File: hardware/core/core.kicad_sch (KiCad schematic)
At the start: 66 parts, among them IC1 LD1117-3.3V-SOT223, J1 9V_IN, J2 MIDI IN, J3 MIDI OUT 1, J4 MIDI OUT 2, J5 MIDI OUT 3, J6 MIDI OUT 4, J7 LCD, J8 USB_C_Receptacle_USB2.0_16P, SW1 FS, SW10 BOOT, SW2 FS, SW3 FS, SW4 FS, SW5 FS, SW6 FS, SW7 FS, SW8 FS, SW9 RESET, U1 LM2596S-5, U2 6N137, U3 ESP32-S3-WROOM-1, U5 USBLC6-2SC6

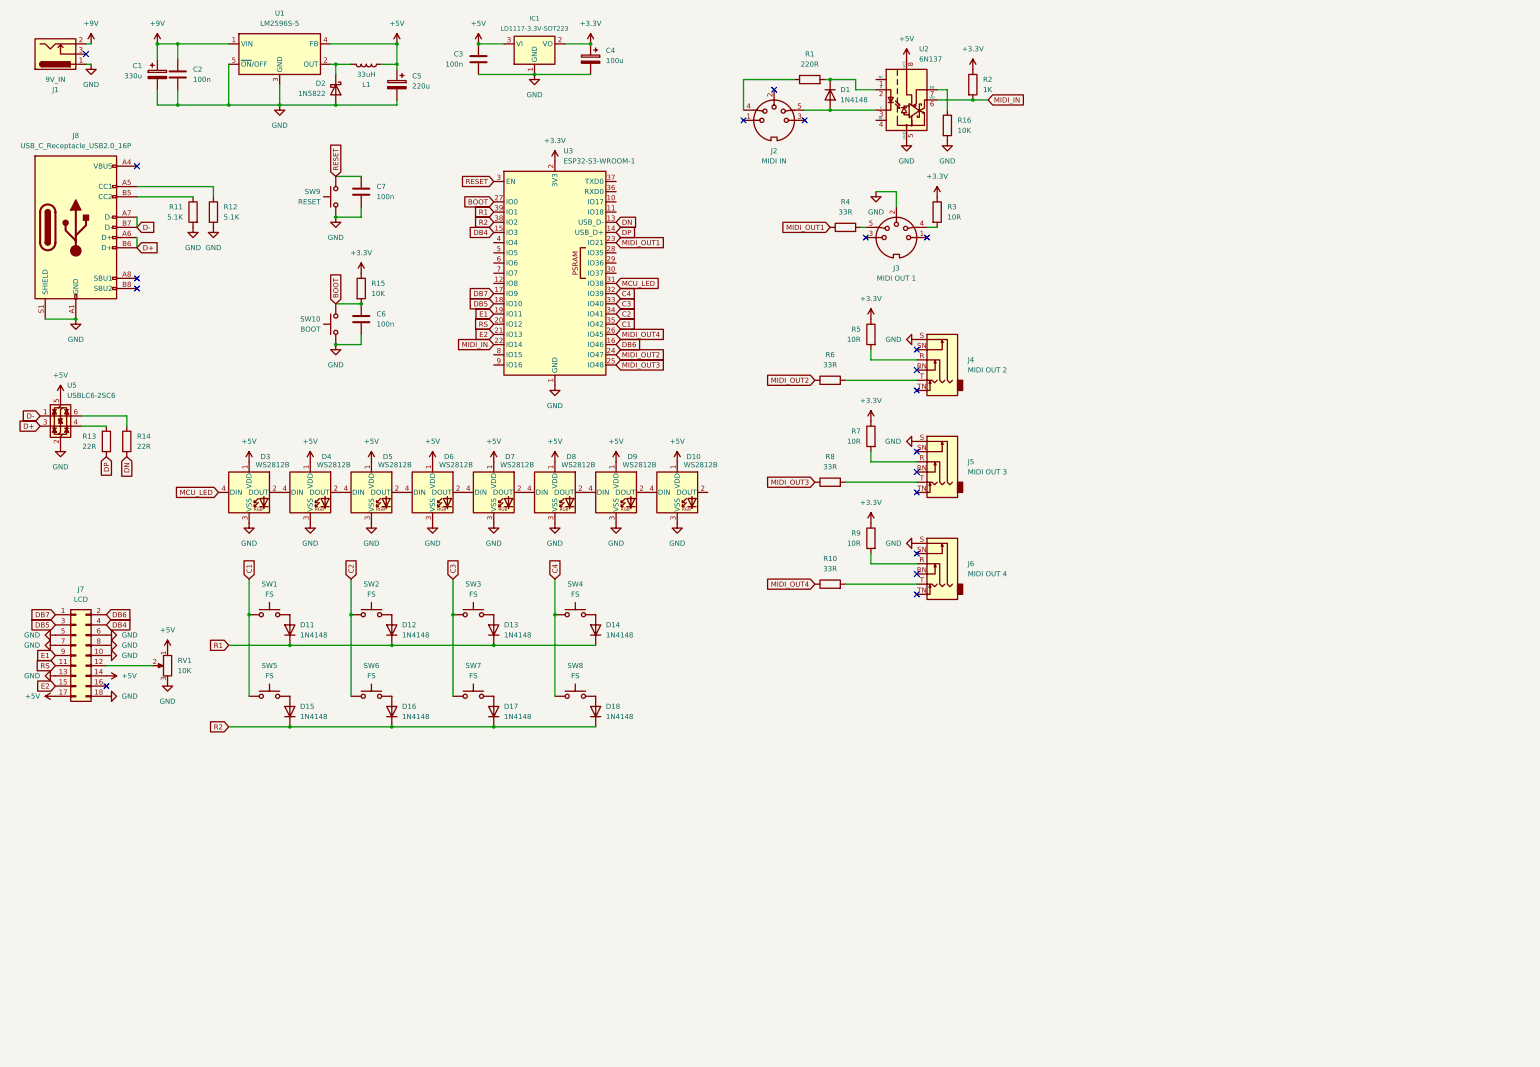
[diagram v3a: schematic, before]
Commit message: Add WS2812B LED support, update LCD pinout docs, and revise PCB nets
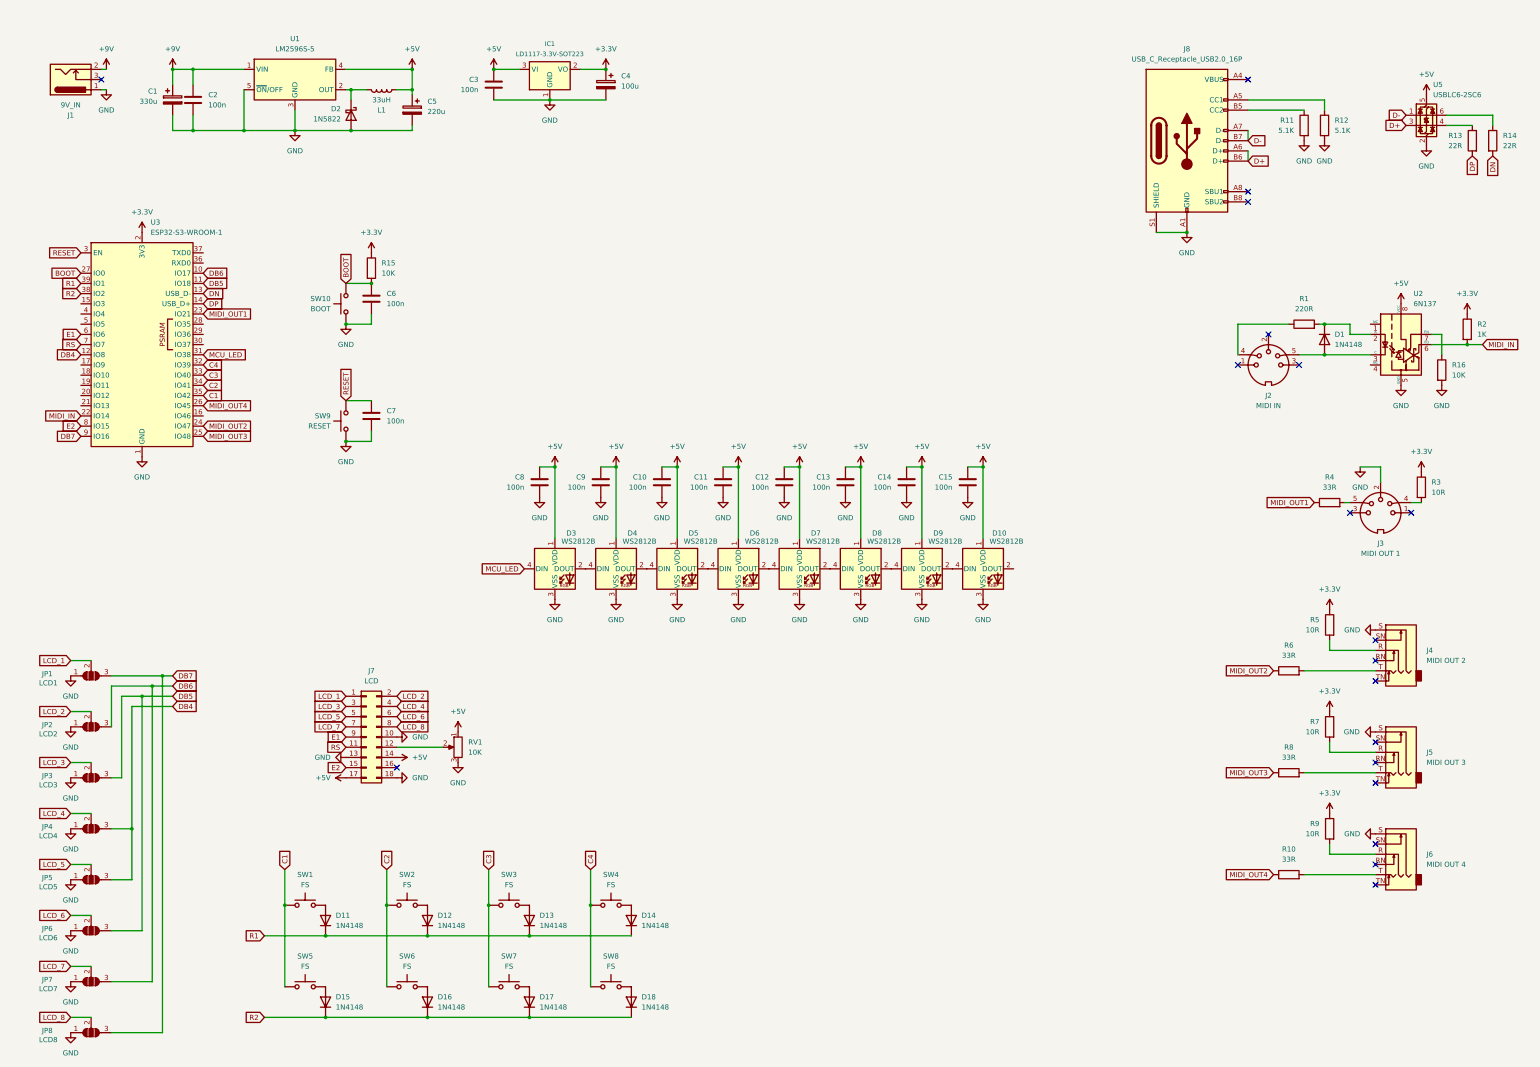
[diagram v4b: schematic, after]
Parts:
- added C10, C11, C12, C13, C14, C15, C8, C9: 100n, Capacitor_THT:C_Rect_L7.0mm_W2.5mm_P5.00mm, symbol Device:C
- added JP1: LCD1, Jumper:SolderJumper-3_P1.3mm_Open_RoundedPad1.0x1.5mm, symbol Jumper:SolderJumper_3_Open
- added JP2: LCD2, Jumper:SolderJumper-3_P1.3mm_Open_RoundedPad1.0x1.5mm, symbol Jumper:SolderJumper_3_Open
- added JP3: LCD3, Jumper:SolderJumper-3_P1.3mm_Open_RoundedPad1.0x1.5mm, symbol Jumper:SolderJumper_3_Open
- added JP4: LCD4, Jumper:SolderJumper-3_P1.3mm_Open_RoundedPad1.0x1.5mm, symbol Jumper:SolderJumper_3_Open
- added JP5: LCD5, Jumper:SolderJumper-3_P1.3mm_Open_RoundedPad1.0x1.5mm, symbol Jumper:SolderJumper_3_Open
- added JP6: LCD6, Jumper:SolderJumper-3_P1.3mm_Open_RoundedPad1.0x1.5mm, symbol Jumper:SolderJumper_3_Open
- added JP7: LCD7, Jumper:SolderJumper-3_P1.3mm_Open_RoundedPad1.0x1.5mm, symbol Jumper:SolderJumper_3_Open
- added JP8: LCD8, Jumper:SolderJumper-3_P1.3mm_Open_RoundedPad1.0x1.5mm, symbol Jumper:SolderJumper_3_Open
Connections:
- net +5V: now also C10.1, C11.1, C12.1, C13.1, C14.1, C15.1, C8.1, C9.1
- net DB4: now also U3.12 (IO8), JP4.3 (B), JP5.3 (B); no longer J7.4 (Pin_4), U3.15 (IO3)
- net DB5: now also U3.11 (IO18), JP3.3 (B), JP6.3 (B); no longer J7.3 (Pin_3), U3.18 (IO10)
- net DB6: now also U3.10 (IO17), JP2.3 (B), JP7.3 (B); no longer J7.2 (Pin_2), U3.16 (IO46)
- net DB7: now also U3.9 (IO16), JP1.3 (B), JP8.3 (B); no longer J7.1 (Pin_1), U3.17 (IO9)
- net E1: now also U3.6 (IO6); no longer U3.19 (IO11)
- net E2: now also U3.8 (IO15); no longer U3.21 (IO13)
- net GND: now also C10.2, C11.2, C12.2, C13.2, C14.2, C15.2, C8.2, C9.2, JP1.1 (A), JP2.1 (A), JP3.1 (A), JP4.1 (A), JP5.1 (A), JP6.1 (A), JP7.1 (A), JP8.1 (A); no longer J7.5 (Pin_5), J7.6 (Pin_6), J7.7 (Pin_7), J7.8 (Pin_8)
- net RS: now also U3.7 (IO7); no longer U3.20 (IO12)
- new net LCD_1: J7.1 (Pin_1), JP1.2 (C)
- new net LCD_2: J7.2 (Pin_2), JP2.2 (C)
- new net LCD_3: J7.3 (Pin_3), JP3.2 (C)
- new net LCD_4: J7.4 (Pin_4), JP4.2 (C)
- new net LCD_5: J7.5 (Pin_5), JP5.2 (C)
- new net LCD_6: J7.6 (Pin_6), JP6.2 (C)
- new net LCD_7: J7.7 (Pin_7), JP7.2 (C)
- new net LCD_8: J7.8 (Pin_8), JP8.2 (C)
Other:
- moved on the sheet: C1, C2, C3, C4, C5, C6, C7, D1, D10, D11, D12, D13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

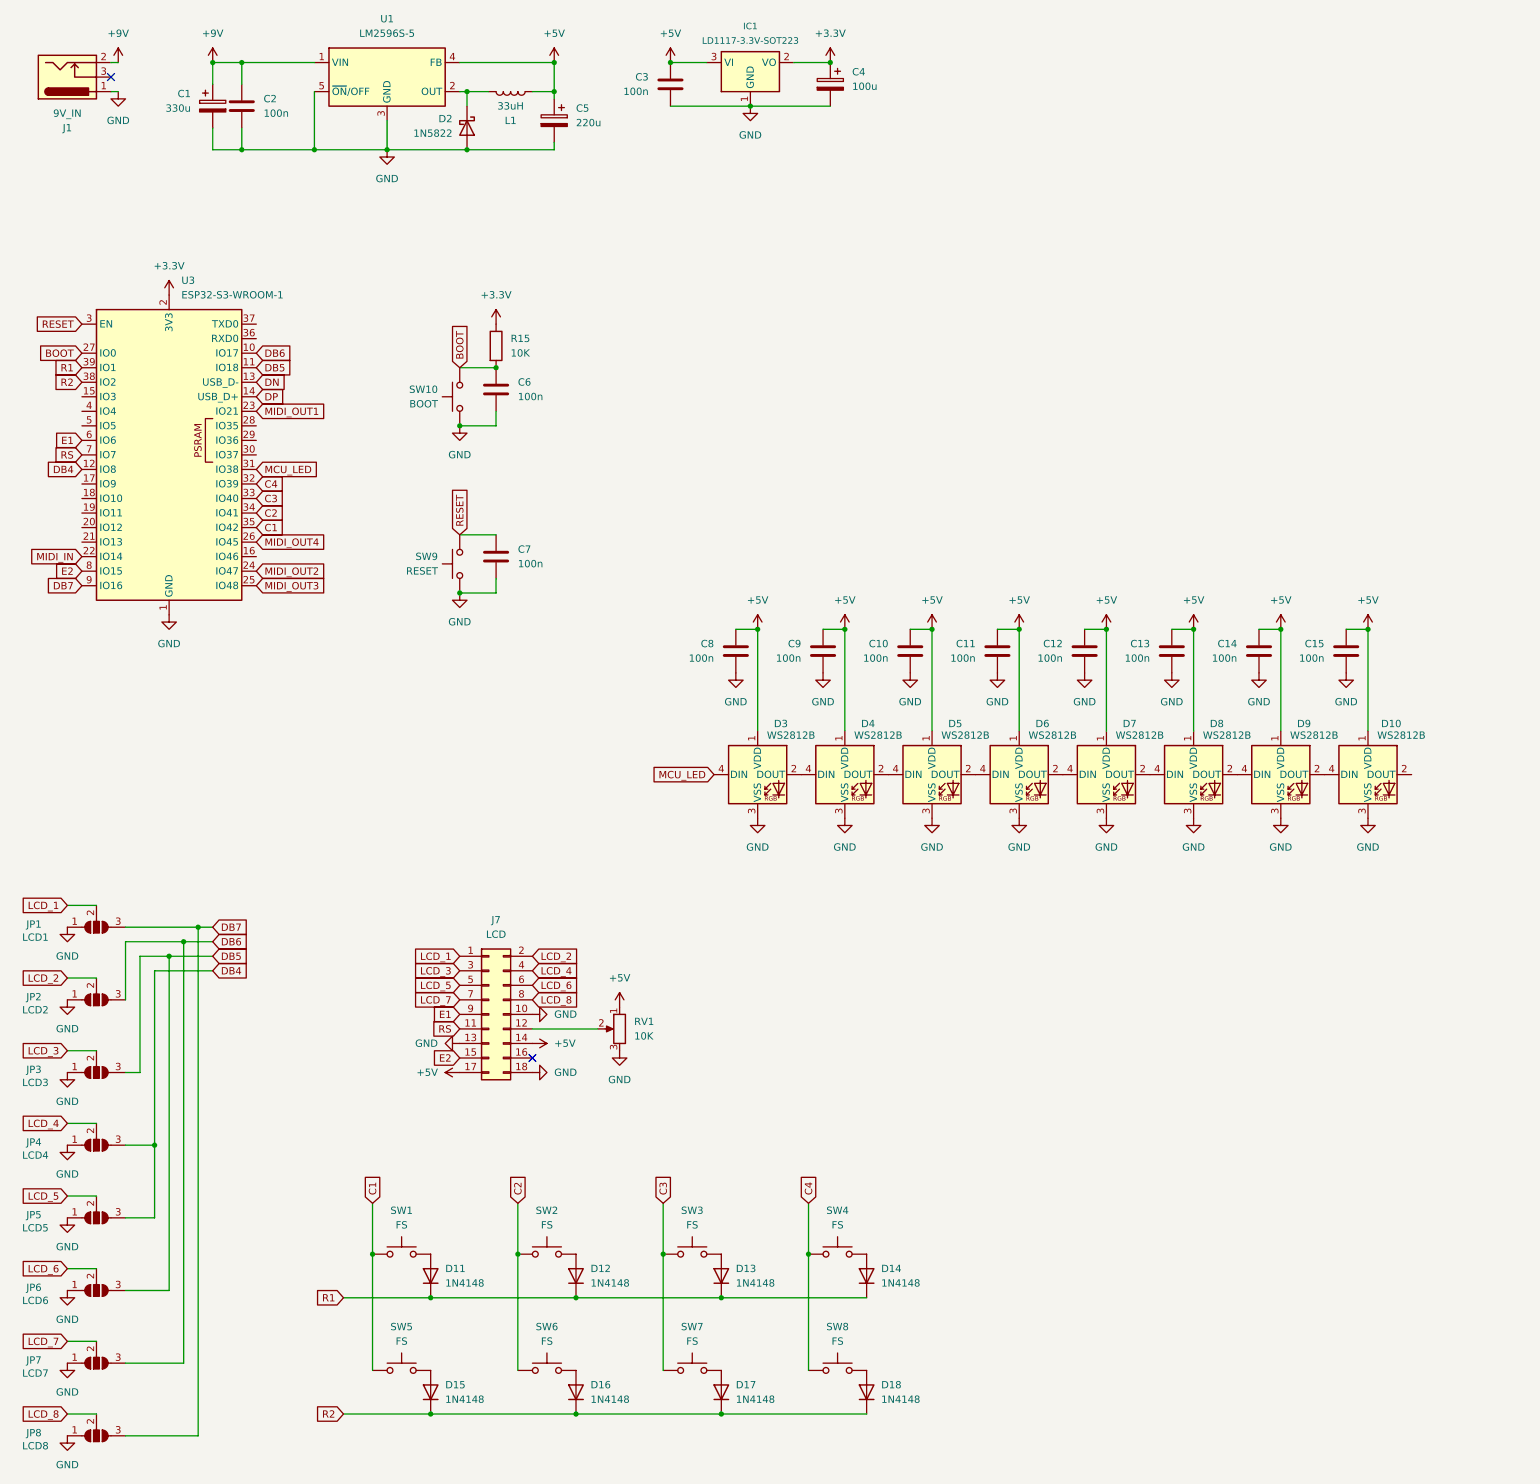
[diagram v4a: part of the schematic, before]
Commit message: Add EMaj logo SVG and silkscreen artwork to PCB
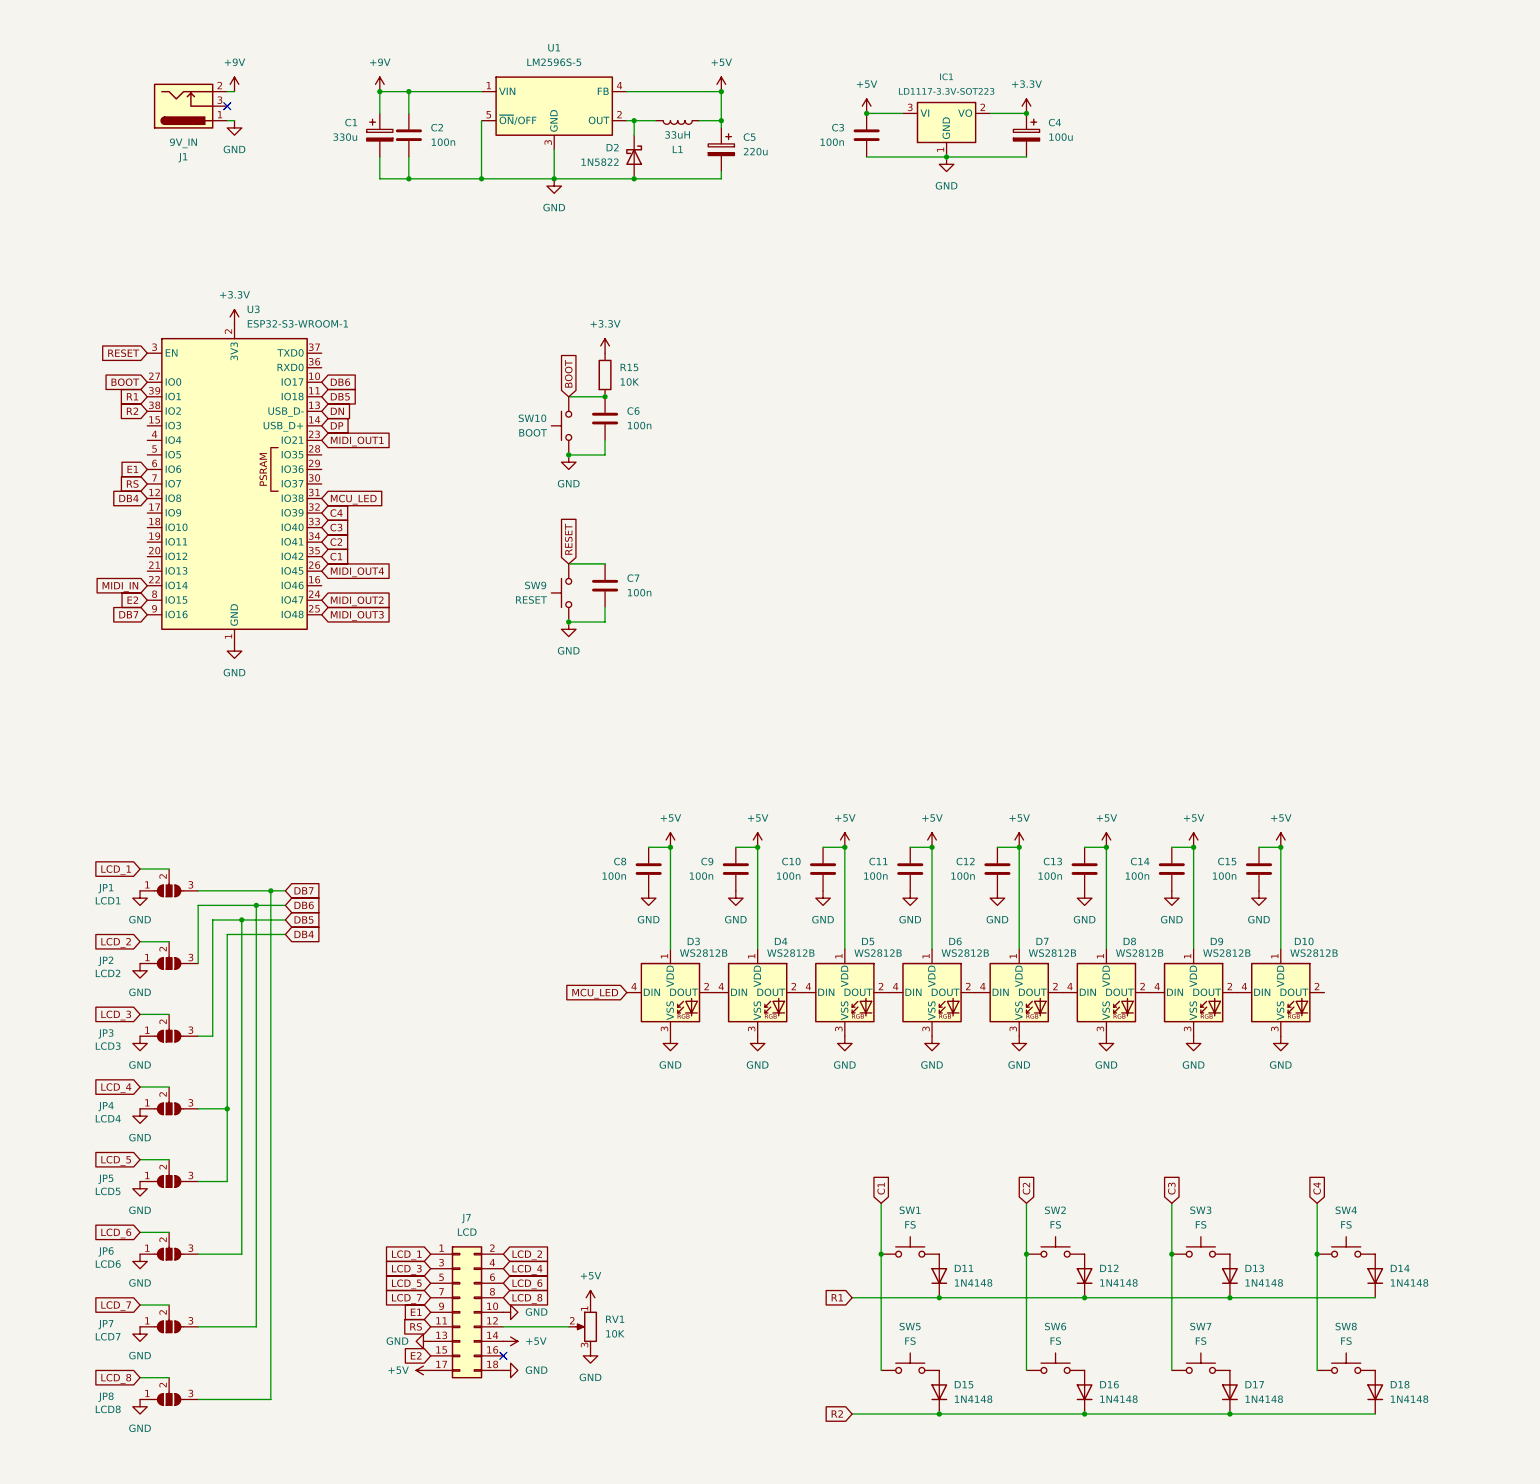
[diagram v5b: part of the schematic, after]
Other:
- moved on the sheet: C1, C10, C11, C12, C13, C14, C15, C2, C3, C4, C5, C6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

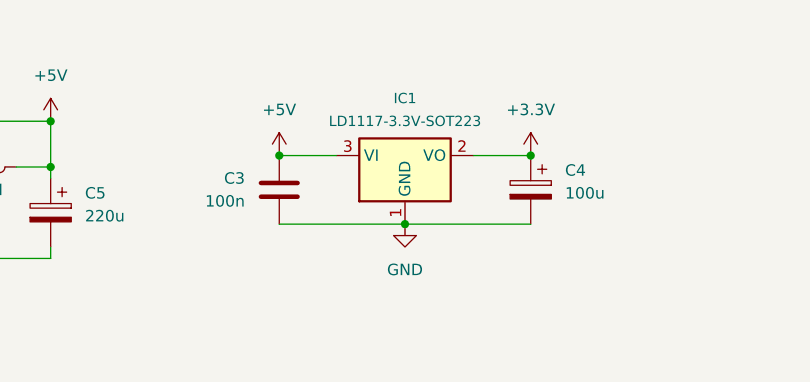
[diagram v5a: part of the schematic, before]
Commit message: Add LCD preset layout diagram and DIN5-180 connector 3D model
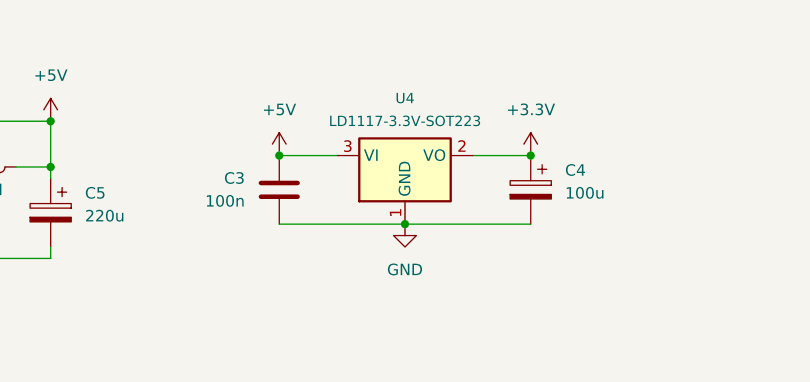
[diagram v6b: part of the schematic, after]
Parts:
- renumbered IC1 to U4
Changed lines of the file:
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@@
 		(dnp no)
 		(fields_autoplaced yes)
-		(property "Reference" "IC1"
+		(property "Reference" "U4"
 			(at 184.15 33.02 0)
 			(effects
@@
 			(project ""
 				(path "/1485bec2-ae99-424e-8aed-104a9db6edd5"
-					(reference "IC1")
+					(reference "U4")
 					(unit 1)
 				)
